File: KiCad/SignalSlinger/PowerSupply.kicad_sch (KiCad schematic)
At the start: 45 parts, among them J201 Barrel_Jack_Switch, J203 External Fan Power, J204 Controlled Fan Power, J205 Controlled Bat Pwr, U201 LP2985-3.3, U202 LP2985-3.3, U203 TO-220 ADJ Reg., U204 TPS22810DBVT, U205 uA7805, U206 TPS22810DBVT

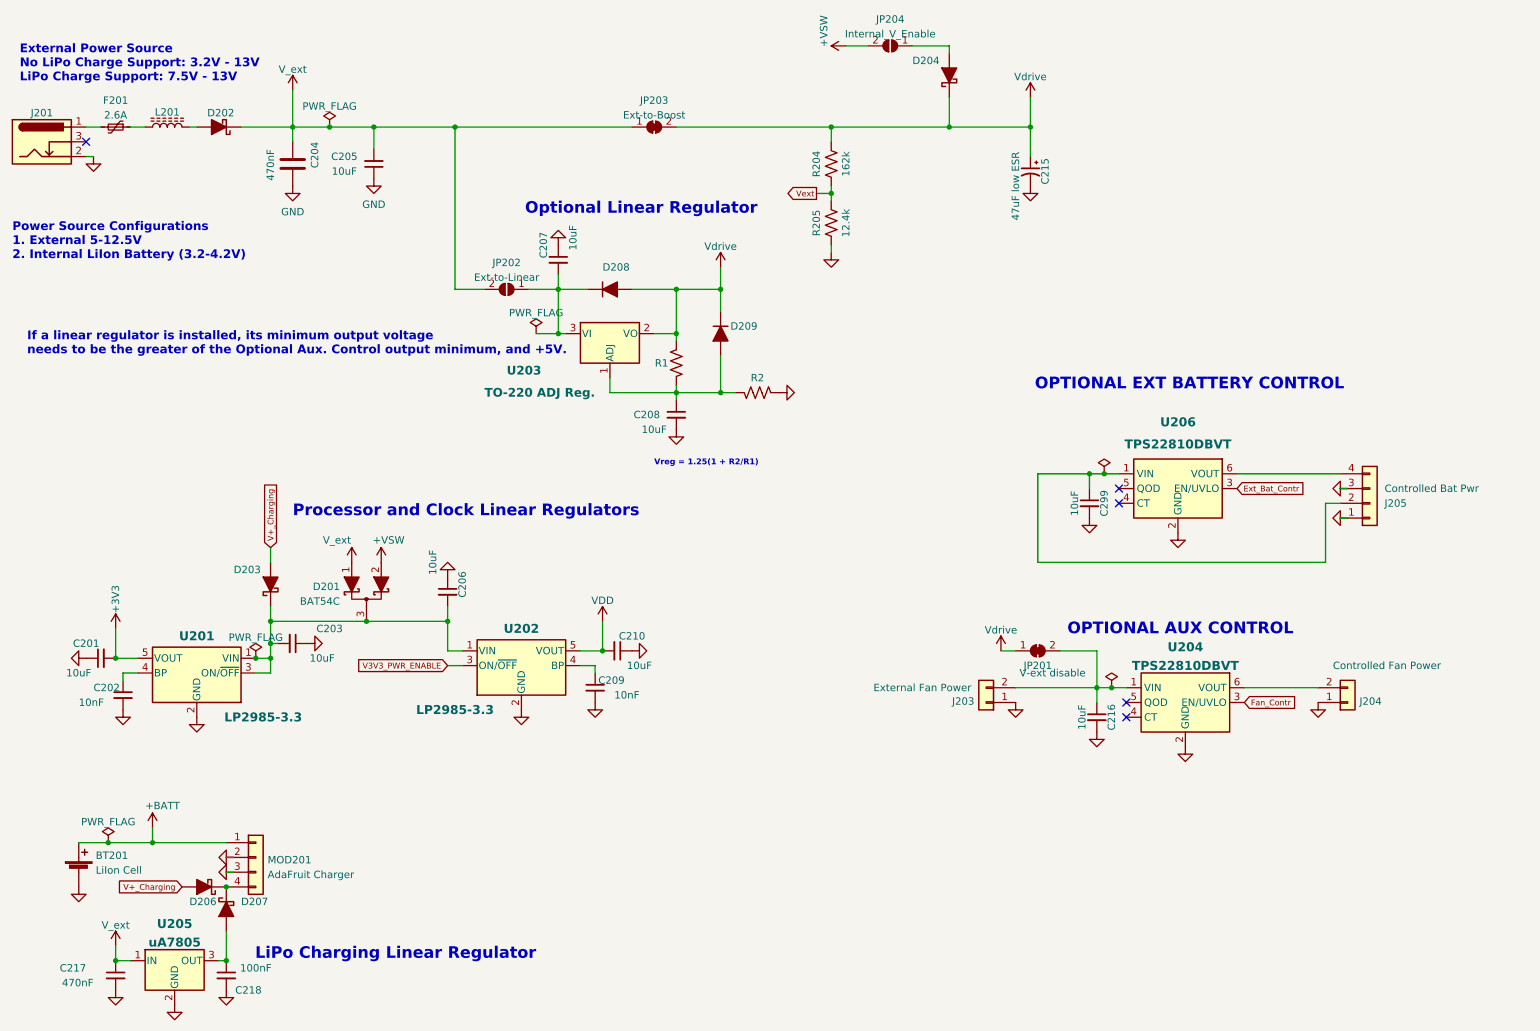
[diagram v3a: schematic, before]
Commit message: Restoring Old KiCad Design
Restoring prototype HW design
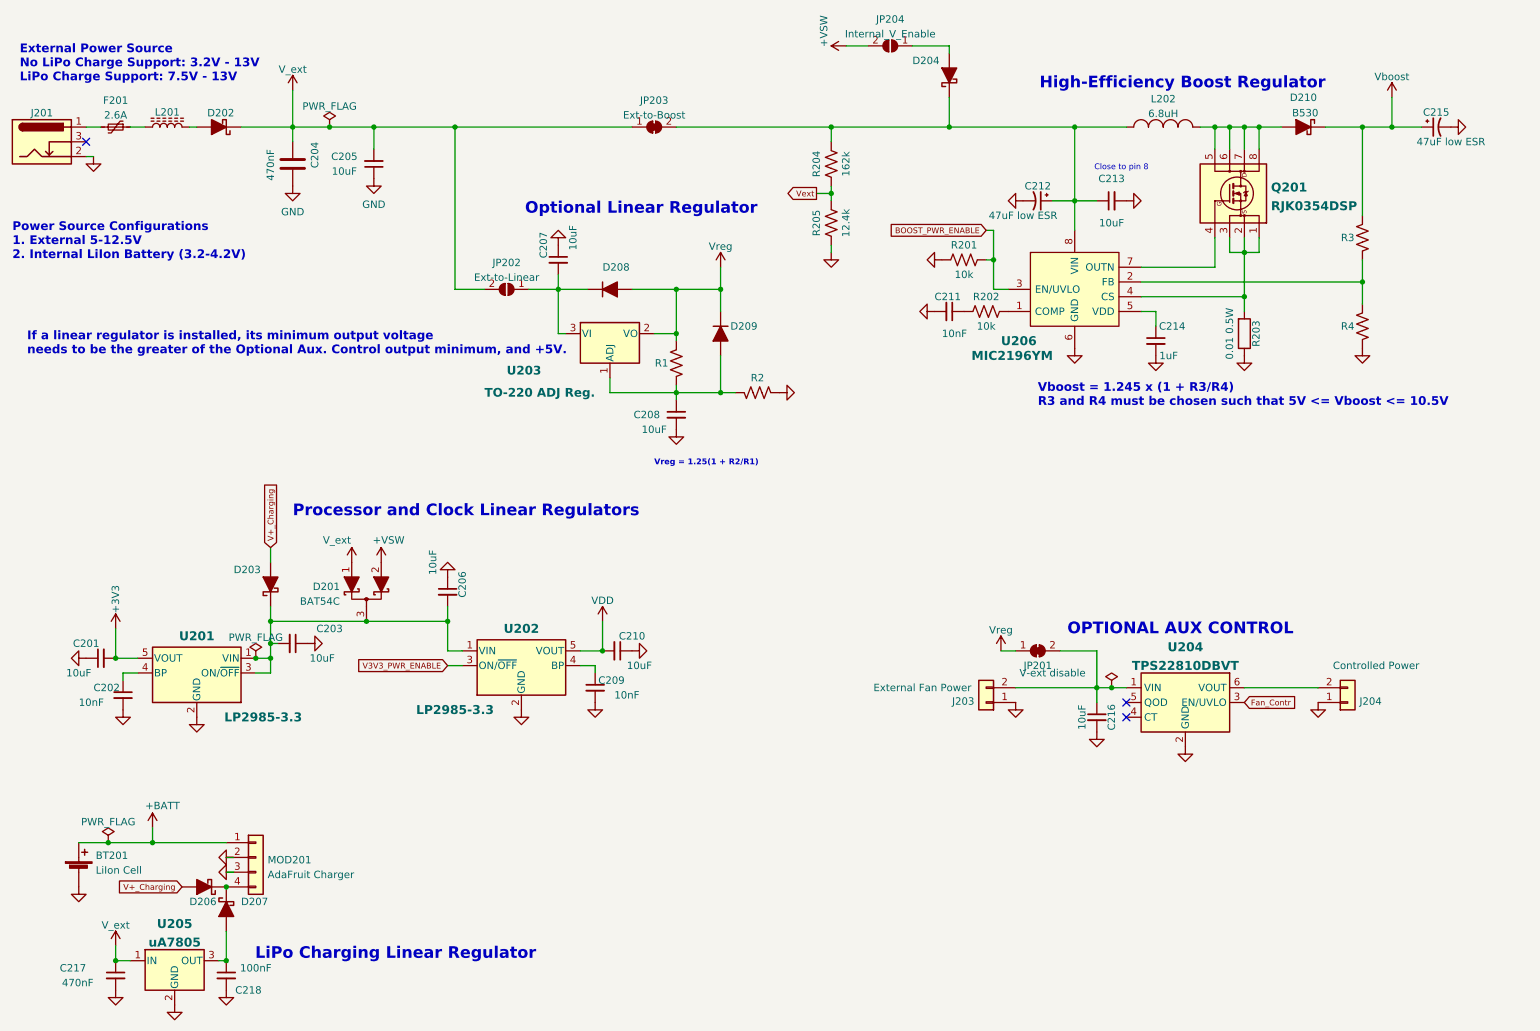
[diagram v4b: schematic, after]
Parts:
- removed C299: 10uF, Capacitor_SMD:C_0805_2012Metric, symbol Device:C_Small
- removed J205: Controlled Bat Pwr, SignalSlinger_Footprints:TerminalBlock_4Ucon_1x02_P3.50mm_Horizontal, symbol SignalSlinger Library:Conn_01x04
- removed U206: TPS22810DBVT, Package_TO_SOT_SMD:SOT-23-6, symbol SignalSlinger Library:TPS22810DBVT
- added C211: 10nF, Capacitor_SMD:C_0805_2012Metric, symbol Device:C_Small
- added C212: 47uF low ESR, Capacitors:C_2917, symbol Device:CP1_Small-Device
- added C213: 10uF, Capacitor_SMD:C_0805_2012Metric, symbol Device:C_Small
- added C214: 1uF, Capacitor_SMD:C_0805_2012Metric, symbol Device:C_Small
- added D210: B530, Diode_SMD:D_SMC, symbol Diode:D_Schottky_B530
- added L202: 6.8uH, Inductors:CDR7D28MN, symbol Device:INDUCTOR_CDR7D28MN
- added Q201: RJK0354DSP, Package_SO:SOIC-8_3.9x4.9mm_P1.27mm, symbol Transistor_FET:RJK0354DSP
- added R201, R202: 10k, Resistor_SMD:R_0805_2012Metric, symbol Device:R_Small_US
- added R203: 0.01 0.5W, Resistor_SMD:R_0805_2012Metric, symbol Device:R
- added R3, R4: TBD, Resistor_THT:R_Axial_DIN0204_L3.6mm_D1.6mm_P2.54mm_Vertical, symbol Device:R_Small_US
- added U206: MIC2196YM, Package_SO:SOIC-8_3.9x4.9mm_P1.27mm, symbol Regulator_Switching:MIC2196YM
- BT201: symbol SignalSlinger Library:Battery_Cell -> Device:Battery_Cell
- C215: footprint SignalSlinger_Footprints:C_2917 -> Capacitors:C_2917; symbol SignalSlinger Library:CP1_Small-Device -> Device:CP1_Small-Device
- D201: symbol SignalSlinger Library:D_Schottky_Dual_CommonCathode_AAK_Parallel -> Device:D_Schottky_Dual_CommonCathode_AAK_Parallel
- D202: symbol SignalSlinger Library:D_Schottky_Filled -> Device:D_Schottky_Filled
- D203, D204, D206, D207: footprint SignalSlinger_Footprints:D_SOD-123FL -> Diode_SMD:D_SOD-123FL; symbol SignalSlinger Library:D_Schottky_Filled -> Device:D_Schottky_Filled
- D208, D209: symbol SignalSlinger Library:1N914WT -> Diode:1N914WT
- J201: symbol SignalSlinger Library:Barrel_Jack_Switch -> Connector:Barrel_Jack_Switch
- J204: value Controlled Fan Power -> Controlled Power
- JP201, JP203: symbol SignalSlinger Library:SolderJumper_2_Bridged -> Jumper:SolderJumper_2_Bridged
- JP202, JP204: symbol SignalSlinger Library:SolderJumper_2_Open -> Jumper:SolderJumper_2_Open
- L201: footprint SignalSlinger_Footprints:WPN4020H2R2MT -> Inductor_SMD:WPN4020H2R2MT
- MOD201: symbol SignalSlinger Library:Conn_01x04 -> Connector_Generic:Conn_01x04
- R1, R2, R204, R205: symbol SignalSlinger Library:R_Small_US -> Device:R_Small_US
- U204: symbol SignalSlinger Library:TPS22810DBVT -> Power_Management:TPS22810DBVT
- U205: footprint SignalSlinger_Footprints:SOT-223-4 -> Package_TO_SOT_SMD:SOT-223-4
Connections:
- net GND: now also C211.2, C212.2, C213.2, C214.2, R201.1, R203.1, R4.1, U206.6 (GND)
- net Vdrive: now also D210.1 (K), R3.2; no longer D204.1 (K), JP203.2 (B), R204.2
- new net: Q201.1 (S), Q201.2 (S), Q201.3 (S), R203.2, U206.4 (CS)
- new net: Q201.4 (G), U206.7 (OUTN)
- new net: D210.2 (A), L202.1, Q201.5 (D), Q201.6 (D), Q201.7 (D), Q201.8 (D)
- new net: C212.1, C213.1, D204.1 (K), JP203.2 (B), L202.2, R204.2, U206.8 (VIN)
- new net: C211.1, R202.1
- new net: C214.1, U206.5 (VDD)
- new net: R202.2, U206.1 (COMP)
- new net: R3.1, R4.2, U206.2 (FB)
- new net BOOST_PWR_ENABLE: R201.2, U206.3 (EN/UVLO)
- no-connect marks 5 -> 3
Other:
- note added: "Close to pin 8"
- note added: "High-Efficiency Boost Regulator"
- note added: "Vboost = 1.245 x (1 + R3/R4) R3 and R4 must be chosen such that 5V <= Vboost <= 10.5V"
- note removed: "OPTIONAL EXT BATTERY CONTROL"
- moved on the sheet: C215

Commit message: Updated to Latest KiCad Version
Updated files
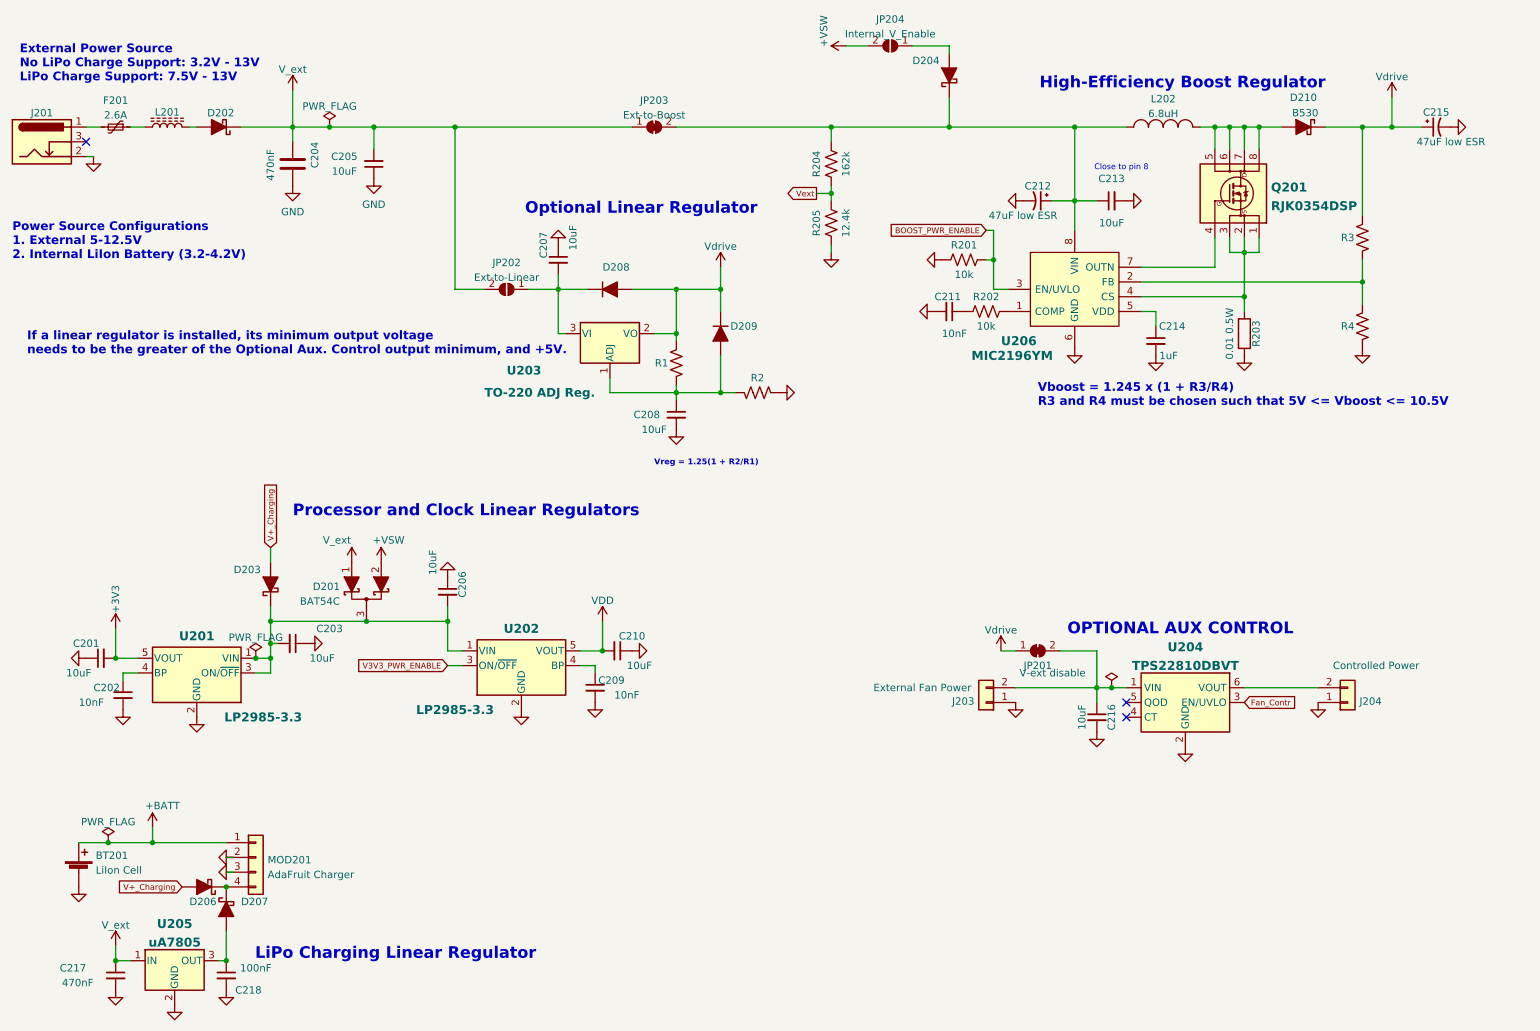
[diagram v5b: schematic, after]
